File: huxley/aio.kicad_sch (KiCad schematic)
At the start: 36 parts, among them J10 SMA, J11 SMA, J12 SMA, J13 SMA, J14 SMA, J15 SMA, J16 SMA, J17 SMA, J6 SMA, J7 SMA, J8 SMA, J9 SMA

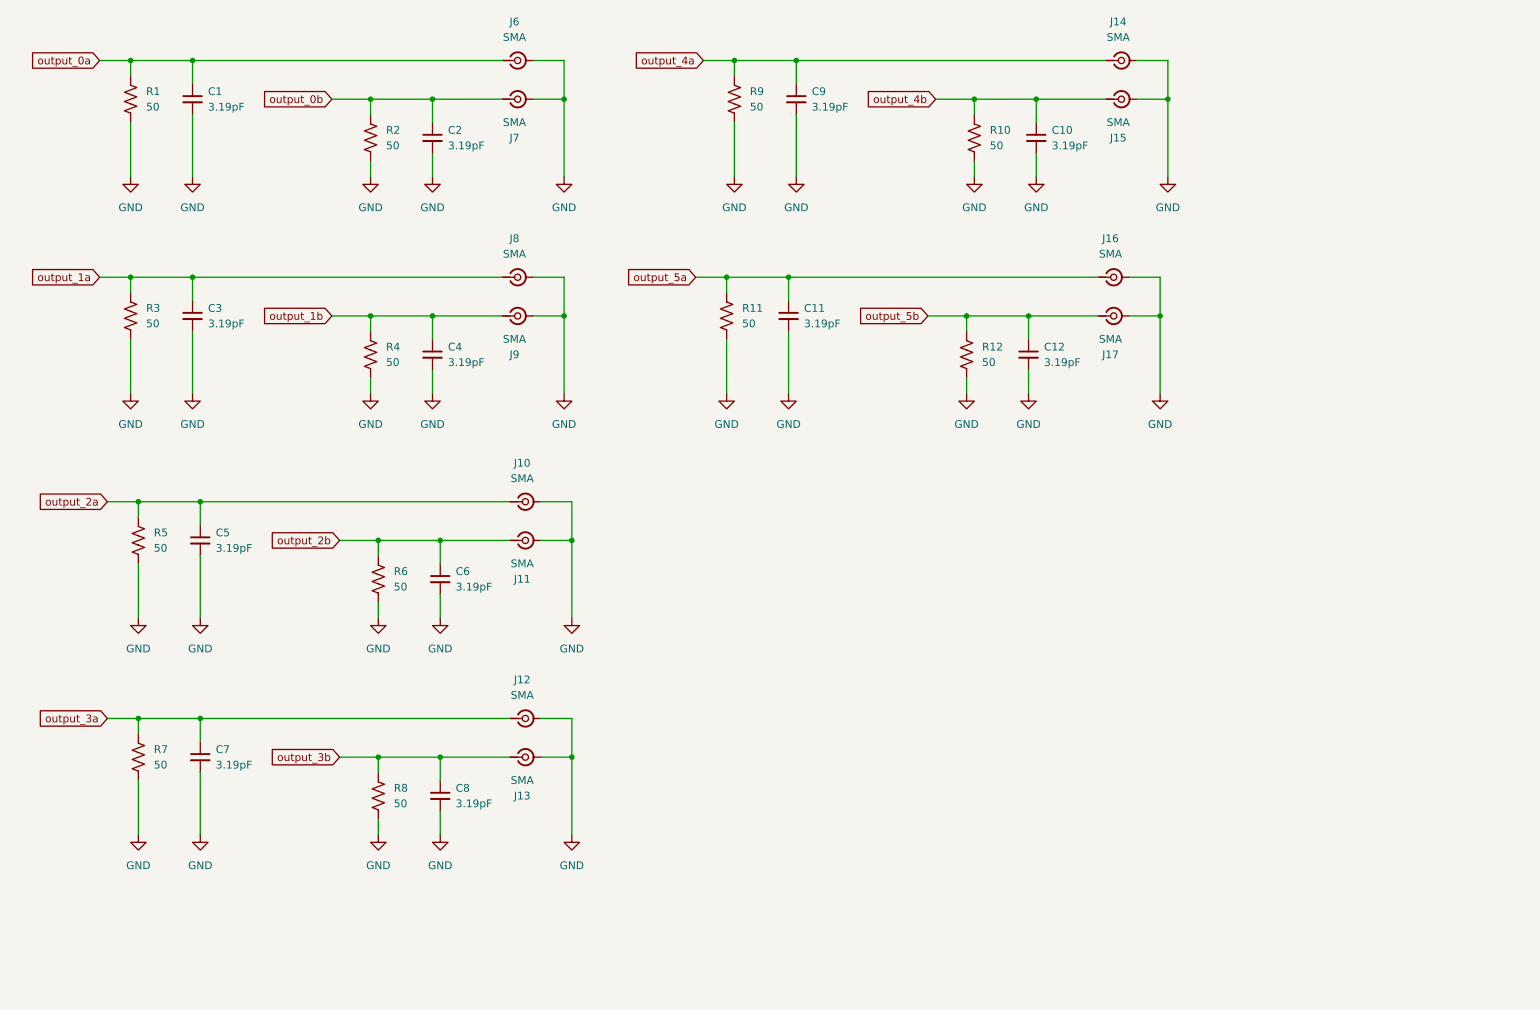
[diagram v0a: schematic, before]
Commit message: added analog chip schematics and connector footprints
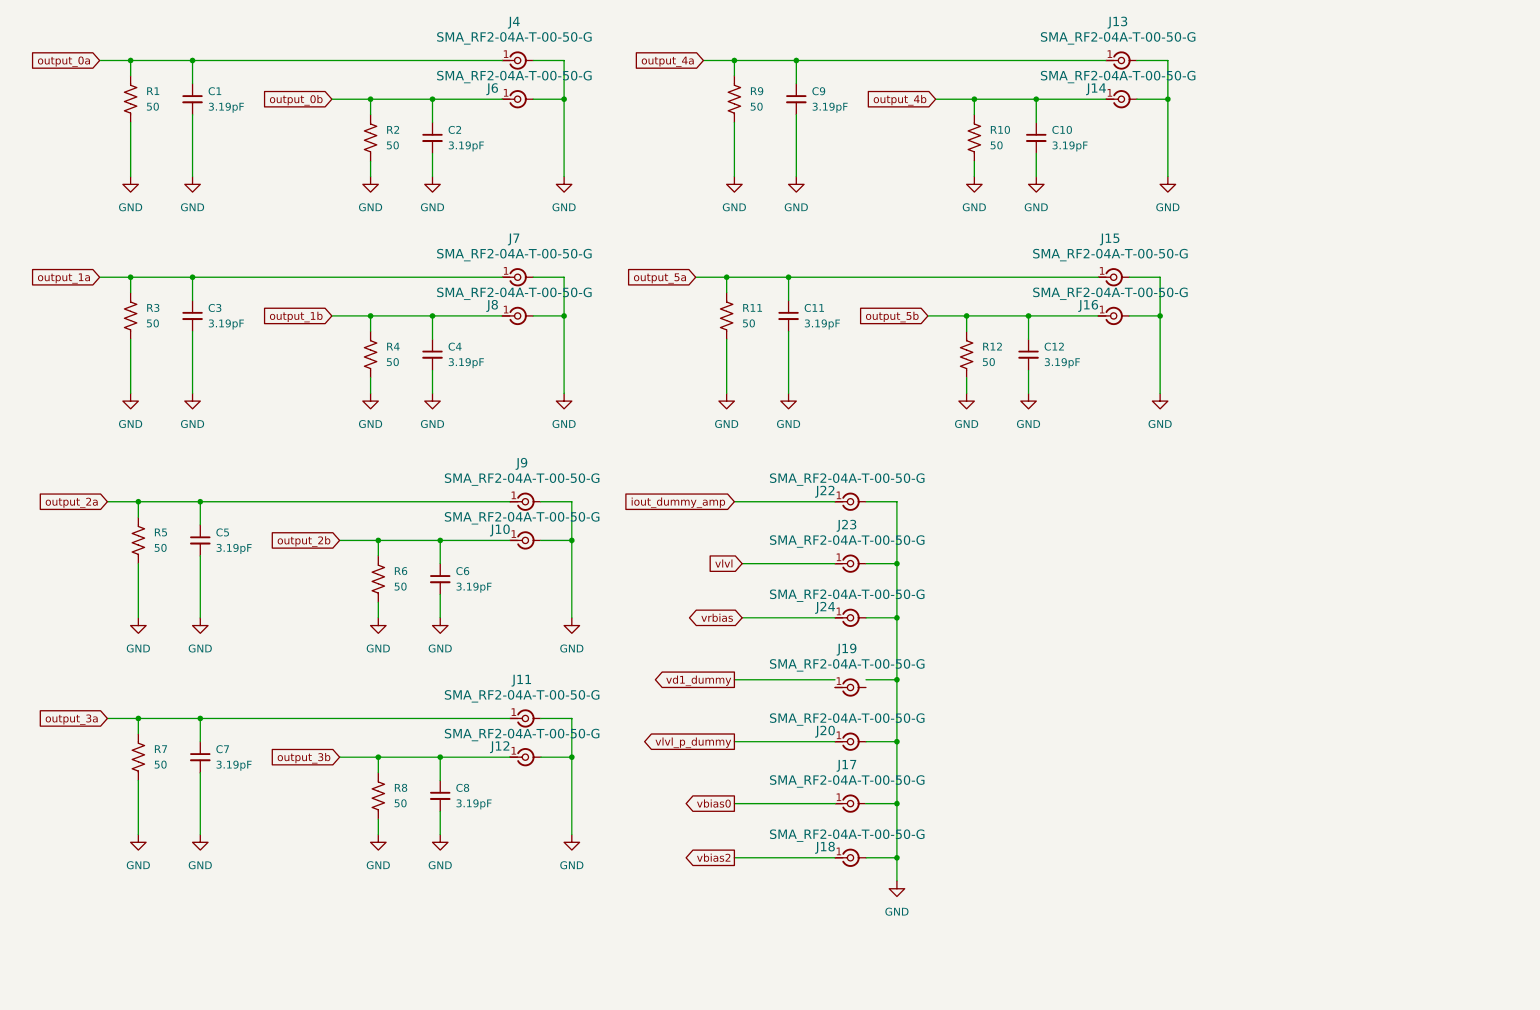
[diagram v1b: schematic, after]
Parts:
- removed J10, J11, J12, J13, J14, J15, J16, J17, J6, J7, J8, J9: SMA, symbol Connector:Conn_Coaxial_Small
- added J10, J11, J12, J13, J14, J15, J16, J17, J18, J19, J20, J22, J23, J24, J4, J6, J7, J8, J9: SMA_RF2-04A-T-00-50-G, 726_footprints:CONN_RF2-04A-T-00-50-G_ADM, symbol _PHASE:SMA_RF2-04A-T-00-50-G
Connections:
- net GND: now also J10., J10.3 (Ext), J10.4 (Ext), J10.5 (Ext), J11., J11.3 (Ext), J11.4 (Ext), J11.5 (Ext), J12., J12.3 (Ext), J12.4 (Ext), J12.5 (Ext), J13., J13.3 (Ext), J13.4 (Ext), J13.5 (Ext), J14., J14.3 (Ext), J14.4 (Ext), J14.5 (Ext), J15., J15.3 (Ext), J15.4 (Ext), J15.5 (Ext), J16., J16.3 (Ext), J16.4 (Ext), J16.5 (Ext), J17., J17.3 (Ext), J17.4 (Ext), J17.5 (Ext), J18., J18.3 (Ext), J18.4 (Ext), J18.5 (Ext), J20., J20.3 (Ext), J20.4 (Ext), J20.5 (Ext), J22., J22.3 (Ext), J22.4 (Ext), J22.5 (Ext), J23., J23.3 (Ext), J23.4 (Ext), J23.5 (Ext), J24., J24.3 (Ext), J24.4 (Ext), J24.5 (Ext), J4., J4.3 (Ext), J4.4 (Ext), J4.5 (Ext), J6., J6.3 (Ext), J6.4 (Ext), J6.5 (Ext), J7., J7.3 (Ext), J7.4 (Ext), J7.5 (Ext), J8., J8.3 (Ext), J8.4 (Ext), J8.5 (Ext), J9., J9.3 (Ext), J9.4 (Ext), J9.5 (Ext)
- net output_0a: now also J4.1
- net output_0b: now also J6.1
- net output_1a: now also J7.1
- net output_1b: now also J8.1
- net output_2a: now also J9.1
- net output_2b: now also J10.1
- net output_3a: now also J11.1
- net output_3b: now also J12.1
- net output_4a: now also J13.1
- net output_4b: now also J14.1
- net output_5a: now also J15.1
- net output_5b: now also J16.1
- new net: J19., J19.3 (Ext), J19.4 (Ext), J19.5 (Ext)
- new net iout_dummy_amp: J22.1
- new net vbias0: J17.1
- new net vbias2: J18.1
- new net vlvl: J23.1
- new net vlvl_p_dummy: J20.1
- new net vrbias: J24.1

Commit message: updated Ibias gen and footprints
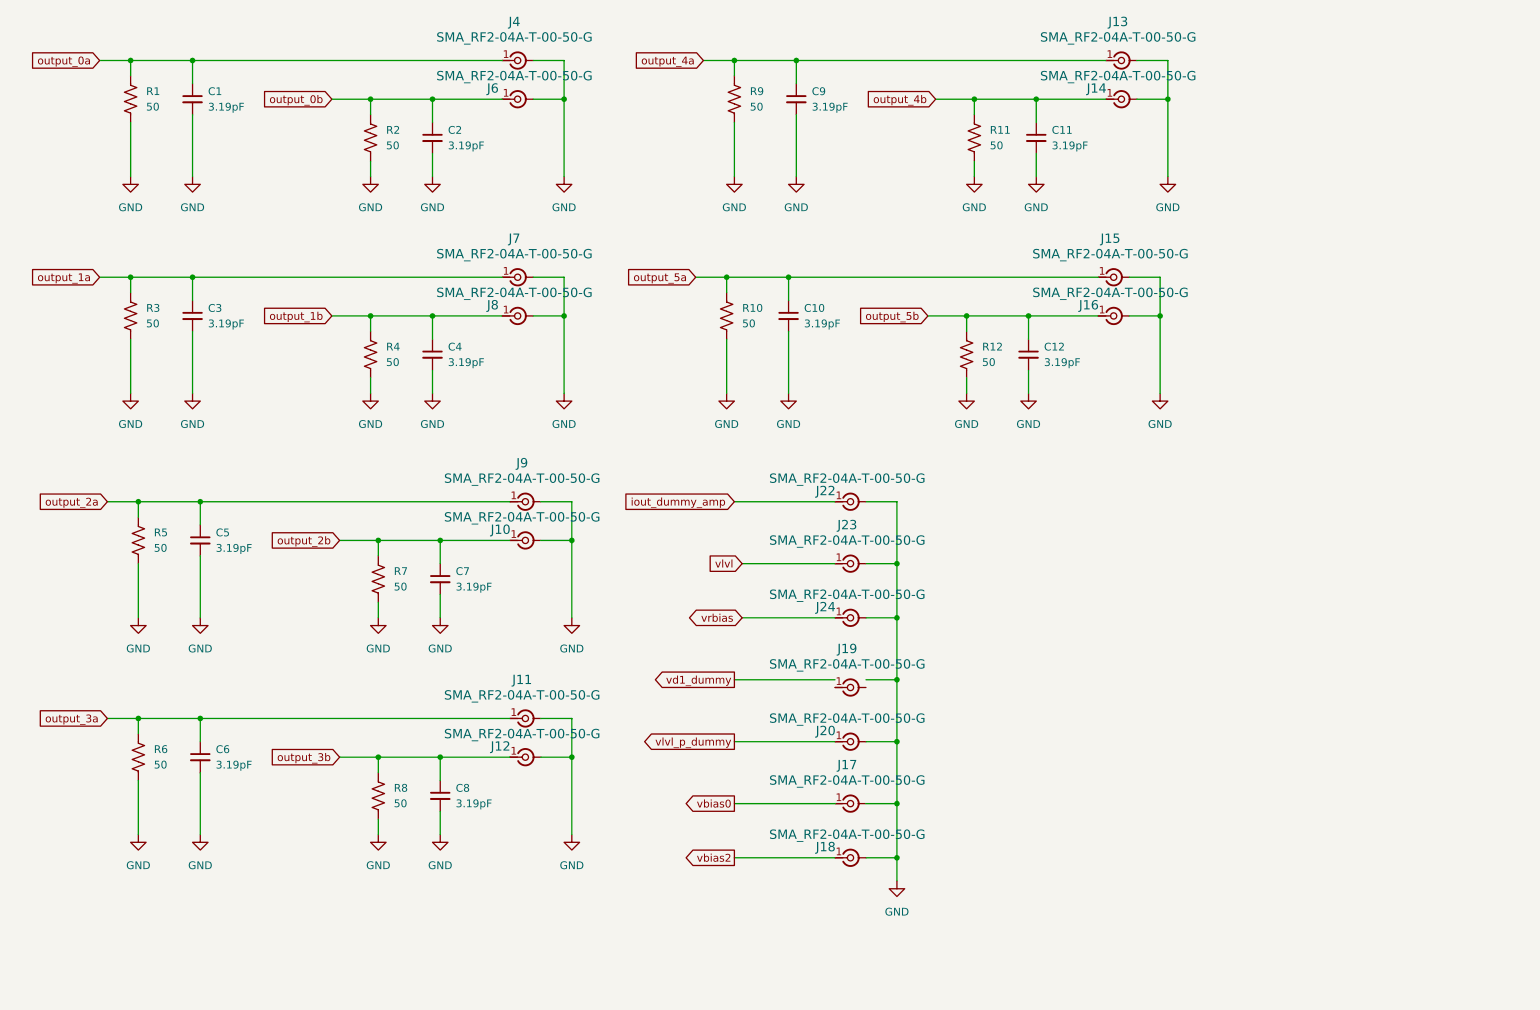
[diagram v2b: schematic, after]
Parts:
- C1, C10, C11, C12, C2, C3, C4, C5, C6, C7, C8, C9: footprint (none) -> Capacitor_SMD:C_0402_1005Metric
- R1, R10, R11, R12, R2, R3, R4, R5, R6, R7, R8, R9: footprint (none) -> Resistor_SMD:R_2512_6332Metric
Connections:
- net output_2b: now also C7.1, R7.1; no longer C6.1, R6.1
- net output_3a: now also C6.1, R6.1; no longer C7.1, R7.1
- net output_4b: now also C11.1, R11.1; no longer C10.1, R10.1
- net output_5a: now also C10.1, R10.1; no longer C11.1, R11.1

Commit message: updated footprints
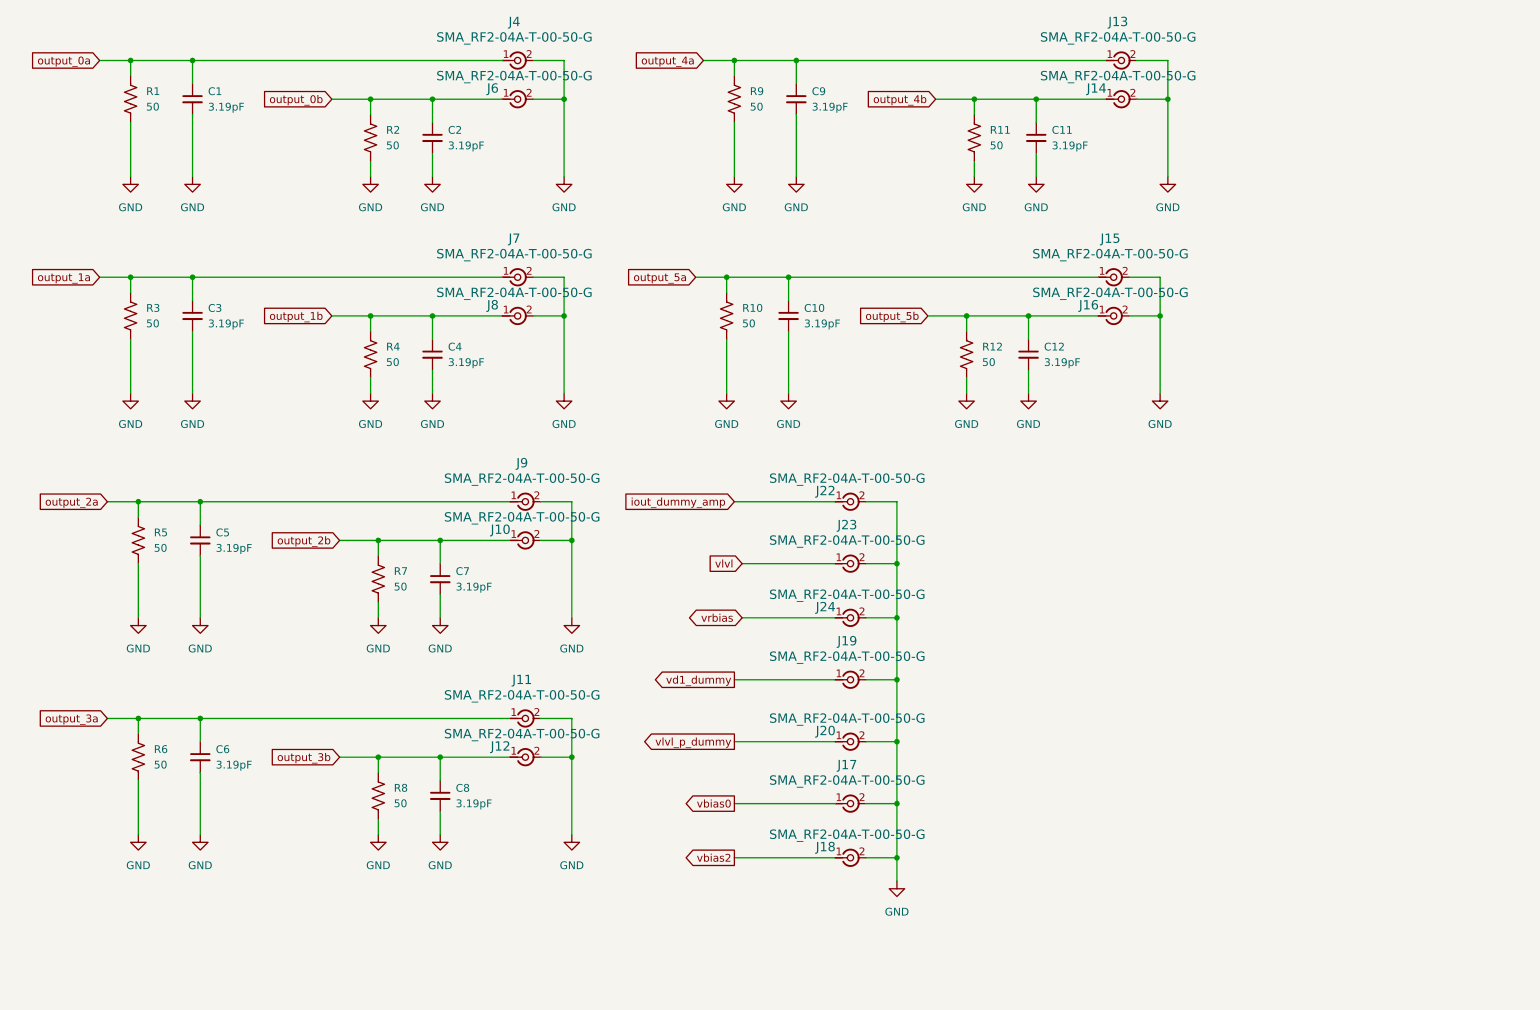
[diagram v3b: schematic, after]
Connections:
- net GND: now also J10.2, J11.2, J12.2, J13.2, J14.2, J15.2, J16.2, J17.2, J18.2, J19.2, J19.3 (Ext), J19.4 (Ext), J19.5 (Ext), J20.2, J22.2, J23.2, J24.2, J4.2, J6.2, J7.2, J8.2, J9.2; no longer J10., J11., J12., J13., J14., J15., J16., J17., J18., J20., J22., J23., J24., J4., J6., J7., J8., J9.
- net vd1_dummy: now also J19.1
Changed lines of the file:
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@@
 			)
 		)
-		(pin ""
+		(pin "2"
 		)
 		(pin "3"
@@
 			)
 		)
-		(pin ""
+		(pin "2"
 		)
 		(pin "3"
@@
 			)
 		)
-		(pin ""
+		(pin "2"
 		)
 		(pin "3"
@@
 			)
 		)
-		(pin ""
+		(pin "2"
 		)
 		(pin "3"
@@
 	(symbol
 		(lib_id "_PHASE:SMA_RF2-04A-T-00-50-G")
-		(at 149.86 129.54 0)
+		(at 149.86 128.27 0)
 		(unit 1)
 		(exclude_from_sim no)
@@
 		(fields_autoplaced yes)
 		(property "Reference" "J19"
-			(at 162.0404 128.27 0)
+			(at 162.0404 127 0)
 			(effects
 				(font
@@
 		)
 		(property "Value" "SMA_RF2-04A-T-00-50-G"
-			(at 162.0404 130.81 0)
+			(at 162.0404 129.54 0)
 			(effects
 				(font
@@
 		)
 		(property "Footprint" "726_footprints:CONN_RF2-04A-T-00-50-G_ADM"
-			(at 149.86 129.54 0)
+			(at 149.86 128.27 0)
 			(effects
 				(font
@@
 		)
 		(property "Datasheet" "112404"
-			(at 149.86 129.54 0)
+			(at 149.86 128.27 0)
 			(effects
 				(font
@@
 		)
 		(property "Description" ""
-			(at 149.86 129.54 0)
+			(at 149.86 128.27 0)
 			(effects
 				(font
@@
 			)
 		)
-		(pin ""
+		(pin "2"
 		)
 		(pin "3"
@@
 			)
 		)
-		(pin ""
+		(pin "2"
 		)
 		(pin "3"
@@
 			)
 		)
-		(pin ""
+		(pin "2"
 		)
 		(pin "3"
@@
 			)
 		)
-		(pin ""
+		(pin "2"
 		)
 		(pin "3"
@@
 			)
 		)
-		(pin ""
+		(pin "2"
 		)
 		(pin "3"
@@
 			)
 		)
-		(pin ""
+		(pin "2"
 		)
 		(pin "3"
@@
 			)
 		)
-		(pin ""
+		(pin "2"
 		)
 		(pin "3"
@@
 			)
 		)
-		(pin ""
+		(pin "2"
 		)
 		(pin "3"
@@
 			)
 		)
-		(pin ""
+		(pin "2"
 		)
 		(pin "3"
@@
 			)
 		)
-		(pin ""
+		(pin "2"
 		)
 		(pin "3"
@@
 			)
 		)
-		(pin ""
+		(pin "2"
 		)
 		(pin "3"
@@
 			)
 		)
-		(pin ""
+		(pin "2"
 		)
 		(pin "3"
@@
 			)
 		)
-		(pin ""
+		(pin "2"
 		)
 		(pin "3"
@@
 			)
 		)
-		(pin ""
+		(pin "2"
 		)
 		(pin "3"
@@
 			)
 		)
-		(pin ""
+		(pin "2"
 		)
 		(pin "3"

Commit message: layout
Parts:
- added C36, C40: 10u, Capacitor_SMD:C_0402_1005Metric, symbol pspice:C
- added C37, C41: 0.1u, Capacitor_SMD:C_0402_1005Metric, symbol pspice:C
- added C38, C42: 1n, Capacitor_SMD:C_0402_1005Metric, symbol pspice:C
- added C39, C43: 10p, Capacitor_SMD:C_0402_1005Metric, symbol pspice:C
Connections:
- net GND: now also C36.2, C37.2, C38.2, C39.2, C40.2, C41.2, C42.2, C43.2
- net vlvl: now also C40.1, C41.1, C42.1, C43.1
- net vrbias: now also C36.1, C37.1, C38.1, C39.1
